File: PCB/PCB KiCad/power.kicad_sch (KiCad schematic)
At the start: 10 parts, among them U3 LM285D-2.5, U4 AMS1117-3.3

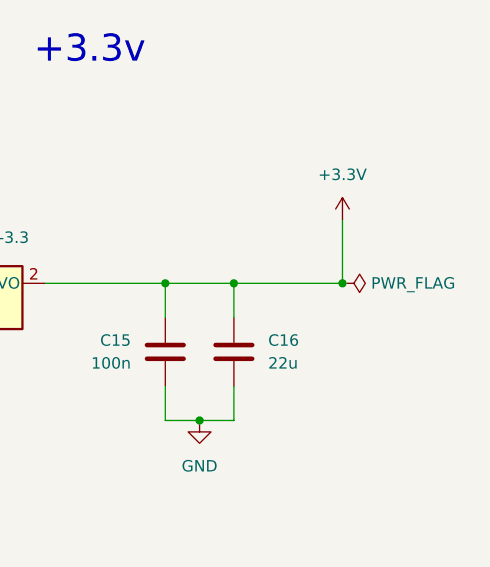
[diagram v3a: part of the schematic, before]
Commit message: Satisfy the overdemanding attention hungry ERC monster
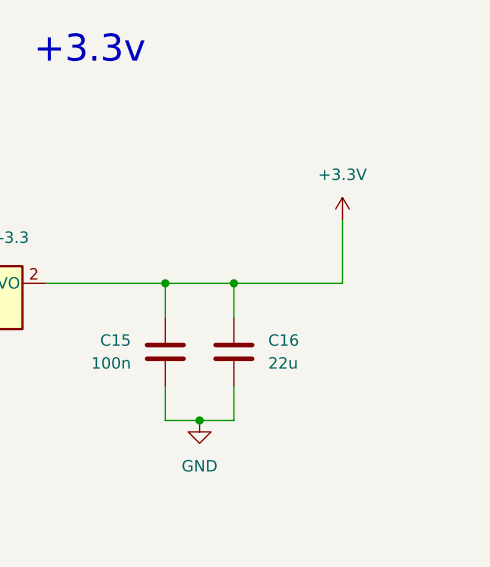
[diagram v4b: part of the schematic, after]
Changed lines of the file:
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@@
   (junction (at 83.82 66.04) (diameter 0) (color 0 0 0 0)
-  )
-  (junction (at 229.87 63.5) (diameter 0) (color 0 0 0 0)
   )
   (junction (at 83.82 76.2) (diameter 0) (color 0 0 0 0)
@@
   (symbol (lib_id "power:PWR_FLAG") (at 100.33 161.29 0) (mirror x) (unit 1)
     (in_bom yes) (on_board yes) (fields_autoplaced)
-    (property "Reference" "#FLG?" (id 0) (at 100.33 163.195 0)
+    (property "Reference" "#FLG0104" (id 0) (at 100.33 163.195 0)
       (effects (font (size 1.27 1.27)) hide)
     )
@@
       (effects (font (size 1.27 1.27)) hide)
     )
-    (pin "1")
-  )
-  (symbol (lib_id "power:PWR_FLAG") (at 229.87 63.5 270) (mirror x) (unit 1)
-    (in_bom yes) (on_board yes) (fields_autoplaced)
-    (property "Reference" "#FLG?" (id 0) (at 231.775 63.5 0)
-      (effects (font (size 1.27 1.27)) hide)
-    )
-    (property "Value" "PWR_FLAG" (id 1) (at 233.045 63.4999 90)
-      (effects (font (size 1.27 1.27)) (justify left))
-    )
-    (property "Footprint" "" (id 2) (at 229.87 63.5 0)
-      (effects (font (size 1.27 1.27)) hide)
-    )
-    (property "Datasheet" "~" (id 3) (at 229.87 63.5 0)
-      (effects (font (size 1.27 1.27)) hide)
-    )

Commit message: Add footprints
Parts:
- FB1: footprint (none) -> Resistor_SMD:R_0805_2012Metric_Pad1.20x1.40mm_HandSolder
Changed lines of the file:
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@@
       (effects (font (size 1.27 1.27)) (justify right))
     )
-    (property "Footprint" "" (id 2) (at 85.598 71.755 90)
+    (property "Footprint" "Resistor_SMD:R_0805_2012Metric_Pad1.20x1.40mm_HandSolder" (id 2) (at 85.598 71.755 90)
       (effects (font (size 1.27 1.27)) hide)
     )

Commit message: export for review
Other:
- company: (none) -> Plastic Scanner
- title: (none) -> Development Board
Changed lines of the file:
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@@
 (kicad_sch (version 20211123) (generator eeschema)
   (paper "A4")
+  (title_block
+    (title "Development Board")
+    (date "2022-03-15")
+    (rev "2.1")
+    (company "Plastic Scanner")
+  )
   (junction (at 210.185 63.5) (diameter 0) (color 0 0 0 0)
   )

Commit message: PCB at time of order
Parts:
- added C15: 10, Capacitor_SMD:C_0805_2012Metric_Pad1.18x1.45mm_HandSolder, symbol Device:C
- renumbered C15 to C16, C16 to C17
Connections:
- net +5V RAW: now also C15.1
- net GND: now also C15.2
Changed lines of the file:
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@@
   (junction (at 108.585 76.2) (diameter 0) (color 0 0 0 0)
   )
+  (junction (at 173.99 63.5) (diameter 0) (color 0 0 0 0)
+  )
   (junction (at 90.17 97.79) (diameter 0) (color 0 0 0 0)
   )
@@
   )
   (wire (pts (xy 210.185 74.93) (xy 210.185 78.74))
+    (stroke (width 0) (type default) (color 0 0 0 0))
+  )
+  (wire (pts (xy 173.99 71.12) (xy 173.99 78.74))
     (stroke (width 0) (type default) (color 0 0 0 0))
   )
@@
   (symbol (lib_id "Device:C") (at 217.805 71.12 0) (unit 1)
     (in_bom yes) (on_board yes) (fields_autoplaced)
-    (property "Reference" "C16" (id 0) (at 221.615 69.8499 0)
+    (property "Reference" "C17" (id 0) (at 221.615 69.8499 0)
       (effects (font (size 1.27 1.27)) (justify left))
     )
@@
   (symbol (lib_id "power:PWR_FLAG") (at 108.585 76.2 0) (mirror x) (unit 1)
     (in_bom yes) (on_board yes) (fields_autoplaced)
-    (property "Reference" "#FLG0101" (id 0) (at 108.585 78.105 0)
+    (property "Reference" "#FLG03" (id 0) (at 108.585 78.105 0)
       (effects (font (size 1.27 1.27)) hide)
     )
@@
   (symbol (lib_id "power:GND") (at 213.995 78.74 0) (unit 1)
     (in_bom yes) (on_board yes) (fields_autoplaced)
-    (property "Reference" "#PWR032" (id 0) (at 213.995 85.09 0)
+    (property "Reference" "#PWR033" (id 0) (at 213.995 85.09 0)
       (effects (font (size 1.27 1.27)) hide)
     )
@@
   (symbol (lib_id "Device:C") (at 210.185 71.12 0) (mirror x) (unit 1)
     (in_bom yes) (on_board yes) (fields_autoplaced)
-    (property "Reference" "C15" (id 0) (at 206.375 69.8499 0)
+    (property "Reference" "C16" (id 0) (at 206.375 69.8499 0)
       (effects (font (size 1.27 1.27)) (justify right))
     )
@@
   (symbol (lib_id "power:PWR_FLAG") (at 100.33 161.29 0) (mirror x) (unit 1)
     (in_bom yes) (on_board yes) (fields_autoplaced)
-    (property "Reference" "#FLG0104" (id 0) (at 100.33 163.195 0)
+    (property "Reference" "#FLG02" (id 0) (at 100.33 163.195 0)
       (effects (font (size 1.27 1.27)) hide)
     )
@@
     (pin "1")
   )
+  (symbol (lib_id "Device:C") (at 173.99 67.31 0) (unit 1)
+    (in_bom yes) (on_board yes) (fields_autoplaced)
+    (property "Reference" "C15" (id 0) (at 177.8 66.0399 0)
+      (effects (font (size 1.27 1.27)) (justify left))
+    )
+    (property "Value" "10" (id 1) (at 177.8 68.5799 0)
+      (effects (font (size 1.27 1.27)) (justify left))
+    )
+    (property "Footprint" "Capacitor_SMD:C_0805_2012Metric_Pad1.18x1.45mm_HandSolder" (id 2) (at 174.9552 71.12 0)
+      (effects (font (size 1.27 1.27)) hide)
+    )
+    (property "Datasheet" "~" (id 3) (at 173.99 67.31 0)
+      (effects (font (size 1.27 1.27)) hide)
+    )
+    (pin "1")
+    (pin "2")
+  )
   (symbol (lib_id "power:+5V") (at 108.585 76.2 0) (unit 1)
     (in_bom yes) (on_board yes) (fields_autoplaced)
@@
   (symbol (lib_id "power:+3.3V") (at 229.87 56.515 0) (unit 1)
     (in_bom yes) (on_board yes) (fields_autoplaced)
-    (property "Reference" "#PWR033" (id 0) (at 229.87 60.325 0)
+    (property "Reference" "#PWR034" (id 0) (at 229.87 60.325 0)
       (effects (font (size 1.27 1.27)) hide)
     )
@@
   (symbol (lib_id "power:GND") (at 189.23 78.74 0) (unit 1)
     (in_bom yes) (on_board yes) (fields_autoplaced)
-    (property "Reference" "#PWR031" (id 0) (at 189.23 85.09 0)
+    (property "Reference" "#PWR032" (id 0) (at 189.23 85.09 0)
       (effects (font (size 1.27 1.27)) hide)
     )
@@
     (pin "1")
   )
+  (symbol (lib_id "power:GND") (at 173.99 78.74 0) (unit 1)
+    (in_bom yes) (on_board yes) (fields_autoplaced)
+    (property "Reference" "#PWR031" (id 0) (at 173.99 85.09 0)
+      (effects (font (size 1.27 1.27)) hide)
+    )
+    (property "Value" "GND" (id 1) (at 173.99 83.82 0))
+    (property "Footprint" "" (id 2) (at 173.99 78.74 0)
+      (effects (font (size 1.27 1.27)) hide)
+    )
+    (property "Datasheet" "" (id 3) (at 173.99 78.74 0)
+      (effects (font (size 1.27 1.27)) hide)
+    )
+    (pin "1")
+  )
   (symbol (lib_id "Device:FerriteBead") (at 83.82 71.755 180) (unit 1)
     (in_bom yes) (on_board yes) (fields_autoplaced)
@@
   (symbol (lib_id "power:PWR_FLAG") (at 90.17 97.79 270) (mirror x) (unit 1)
     (in_bom yes) (on_board yes) (fields_autoplaced)
-    (property "Reference" "#FLG0102" (id 0) (at 92.075 97.79 0)
-      (effects (font (size 1.27 1.27)) hide)
-    )
+    (property "Reference" "#FLG01" (id 0) (at 92.075 97.79 0)
+      (effects (font (size 1.27 1.27)) hide)
+    )

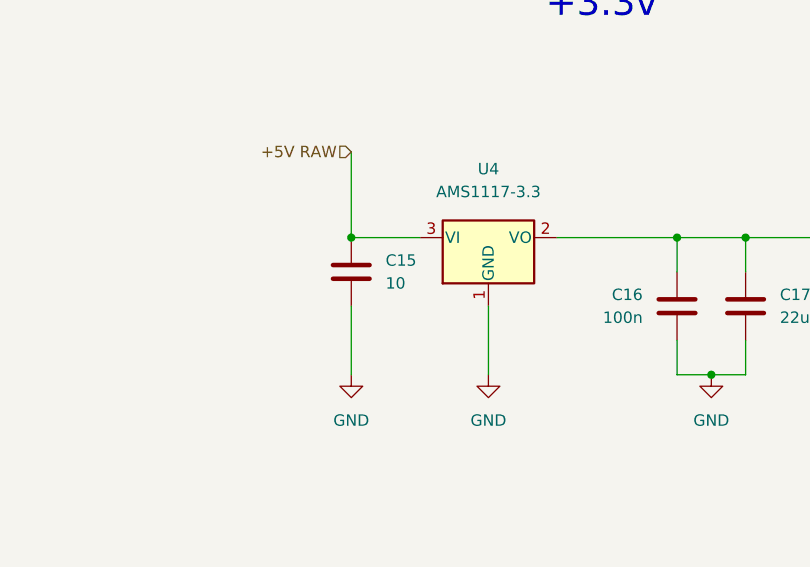
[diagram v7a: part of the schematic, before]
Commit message: Adds 1720nm datasheet and corrects some typ's
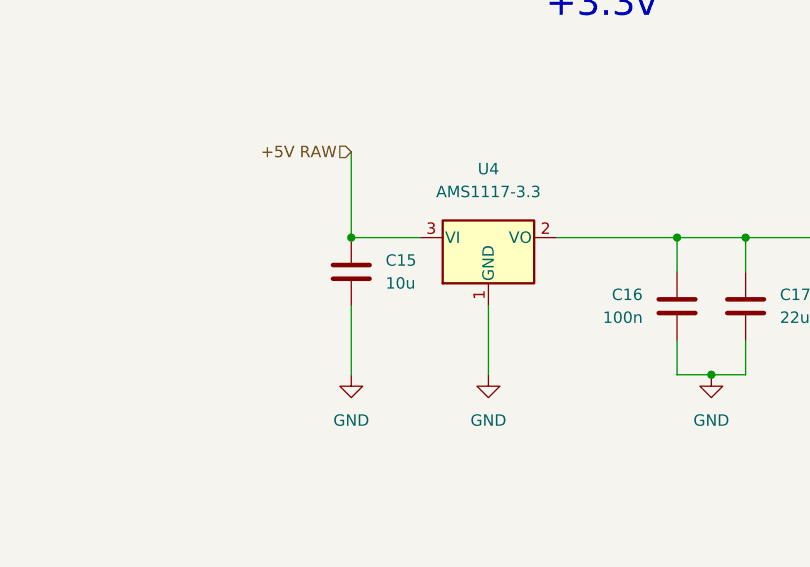
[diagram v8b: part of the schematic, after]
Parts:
- C15: value 10 -> 10u
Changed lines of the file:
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@@
       (effects (font (size 1.27 1.27)) (justify left))
     )
-    (property "Value" "10" (id 1) (at 177.8 68.5799 0)
+    (property "Value" "10u" (id 1) (at 177.8 68.5799 0)
       (effects (font (size 1.27 1.27)) (justify left))
     )
